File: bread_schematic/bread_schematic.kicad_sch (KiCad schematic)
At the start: 4 parts, among them M1 NUCLEO STM32G031K8, U1 SSD1306, U2 TCS34725

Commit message: i lowkey dont know what im doing
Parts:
- U1: value SSD1306 -> SSD1306 128 x 64 OLED (0x3C)
- U2: value TCS34725 -> TCS34725 (0x29)
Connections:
- net SCL: now reaches M1.1 (PB6(D1)), U1.3 (SCL), U2.4 (SCL)
- net SDA: now reaches M1.2 (PB7(D0)), U1.4 (SDA), U2.5 (SDA)
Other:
- company: Jaedyn Carbonell -> NAIT
- title: RGB Reader -> RGB Reader Breadboard Design (Proof of Life)
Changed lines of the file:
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@@
 	(paper "A4")
 	(title_block
-		(title "RGB Reader")
+		(title "RGB Reader Breadboard Design (Proof of Life)")
 		(date "2025-10-21")
-		(company "Jaedyn Carbonell")
+		(company "NAIT")
+		(comment 1 "Jaedyn Carbonell (CMPE2750 Project)")
 	)
 	(junction
@@
 			(type default)
 			(color 255 0 0 1)
+		)
+	)
+	(label "SCL"
+		(at 69.85 33.02 0)
+		(effects
+			(font
+				(size 1.27 1.27)
+			)
+			(justify left bottom)
+		)
+	)
+	(label "SDA"
+		(at 69.85 35.56 0)
+		(effects
+			(font
+				(size 1.27 1.27)
+			)
+			(justify left bottom)
 		)
 	)
@@
 		(dnp no)
 		(property "Reference" "U2"
-			(at 30.48 46.99 0)
-			(effects
-				(font
-					(size 1.27 1.27)
-				)
-				(hide yes)
-			)
-		)
-		(property "Value" "TCS34725"
-			(at 30.226 49.022 0)
+			(at 34.29 60.706 0)
+			(effects
+				(font
+					(size 1.27 1.27)
+				)
+				(hide yes)
+			)
+		)
+		(property "Value" "TCS34725 (0x29)"
+			(at 33.528 49.022 0)
 			(effects
 				(font
@@
 					(size 1.27 1.27)
 				)
+				(hide yes)
 			)
 		)
@@
 		(dnp no)
 		(property "Reference" "U1"
-			(at 33.02 20.32 0)
-			(effects
-				(font
-					(size 1.27 1.27)
-				)
-				(hide yes)
-			)
-		)
-		(property "Value" "SSD1306"
-			(at 29.718 23.876 0)
+			(at 33.02 33.782 0)
+			(effects
+				(font
+					(size 1.27 1.27)
+				)
+				(hide yes)
+			)
+		)
+		(property "Value" "SSD1306 128 x 64 OLED (0x3C)"
+			(at 41.148 23.368 0)
 			(effects
 				(font
@@
 					(size 1.27 1.27)
 				)
+				(hide yes)
 			)
 		)
@@
 			)
 		)
-		(property "Description" "5V USB"
-			(at 79.756 26.162 0)
-			(effects
-				(font
+		(property "Description" "Powered by USB on dev board"
+			(at 89.662 75.184 0)
+			(effects
+				(font

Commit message: oct 22
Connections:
- net SCL: now also U1.4 (SDA)
- net SDA: no longer U1.4 (SDA)
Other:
- note added: "NOTE: 5V --> 3V3 in pcb design"

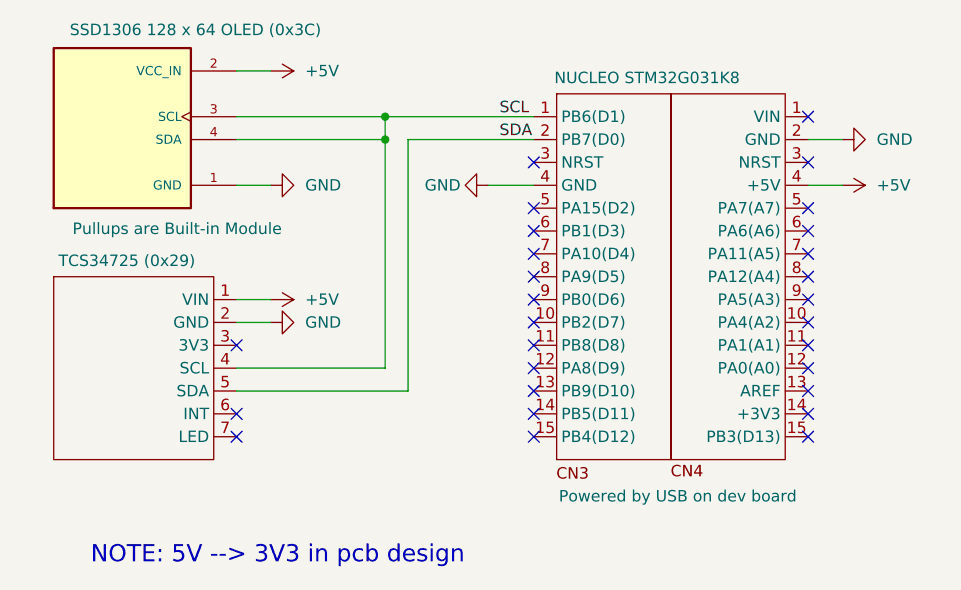
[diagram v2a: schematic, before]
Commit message: Changed after recieving feedback
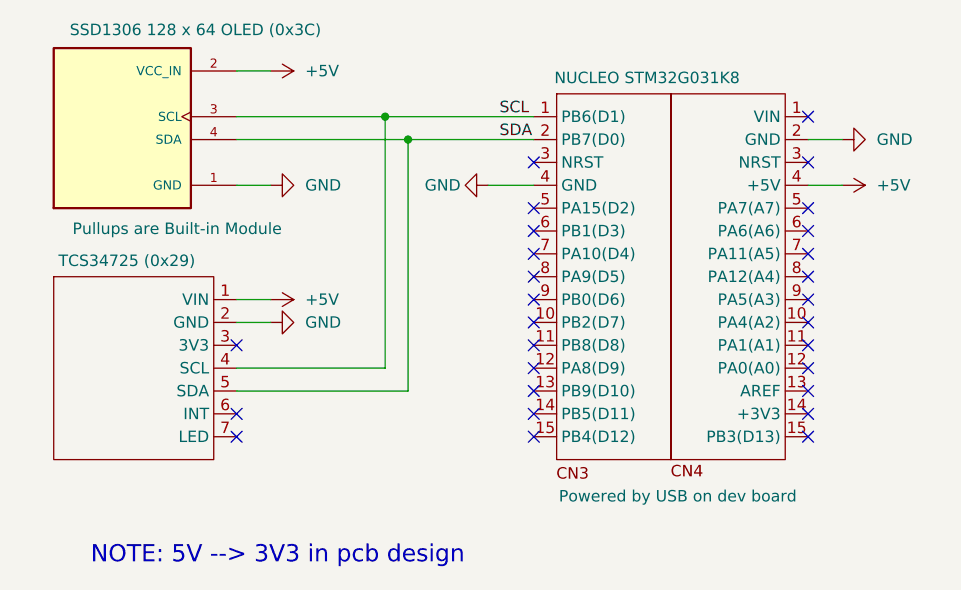
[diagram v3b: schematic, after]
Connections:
- net SCL: no longer U1.4 (SDA)
- net SDA: now also U1.4 (SDA)
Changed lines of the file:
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@@
 		(title "RGB Reader Breadboard Design (Proof of Life)")
 		(date "2025-10-21")
-		(rev "2")
+		(rev "3")
 		(company "NAIT")
 		(comment 1 "Jaedyn Carbonell (CMPE2750 Project)")
@@
 	)
 	(junction
-		(at 57.15 35.56)
+		(at 59.69 35.56)
 		(diameter 0)
 		(color 0 0 0 0)
@@
 	(wire
 		(pts
-			(xy 57.15 60.96) (xy 57.15 35.56)
-		)
-		(stroke
-			(width 0)
-			(type default)
-			(color 0 0 255 1)
-		)
-	)
-	(wire
-		(pts
-			(xy 57.15 35.56) (xy 57.15 33.02)
+			(xy 57.15 33.02) (xy 57.15 60.96)
 		)
 		(stroke
@@
 	(wire
 		(pts
-			(xy 40.64 35.56) (xy 57.15 35.56)
-		)
-		(stroke
+			(xy 40.64 35.56) (xy 59.69 35.56)
+		)
+		(stroke
